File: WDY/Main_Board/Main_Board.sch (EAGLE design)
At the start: 171 parts, among them J1 22-05-7028-02, J10 22-05-7038-03, J11 22-05-7028-02, J12 22-05-7028-02, J13 22-05-7028-02, J14 22-05-7028-02, J15 22-05-7038-03, J2 22-05-7028-02, J3 22-05-7048-04, J4 22-05-7048-04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

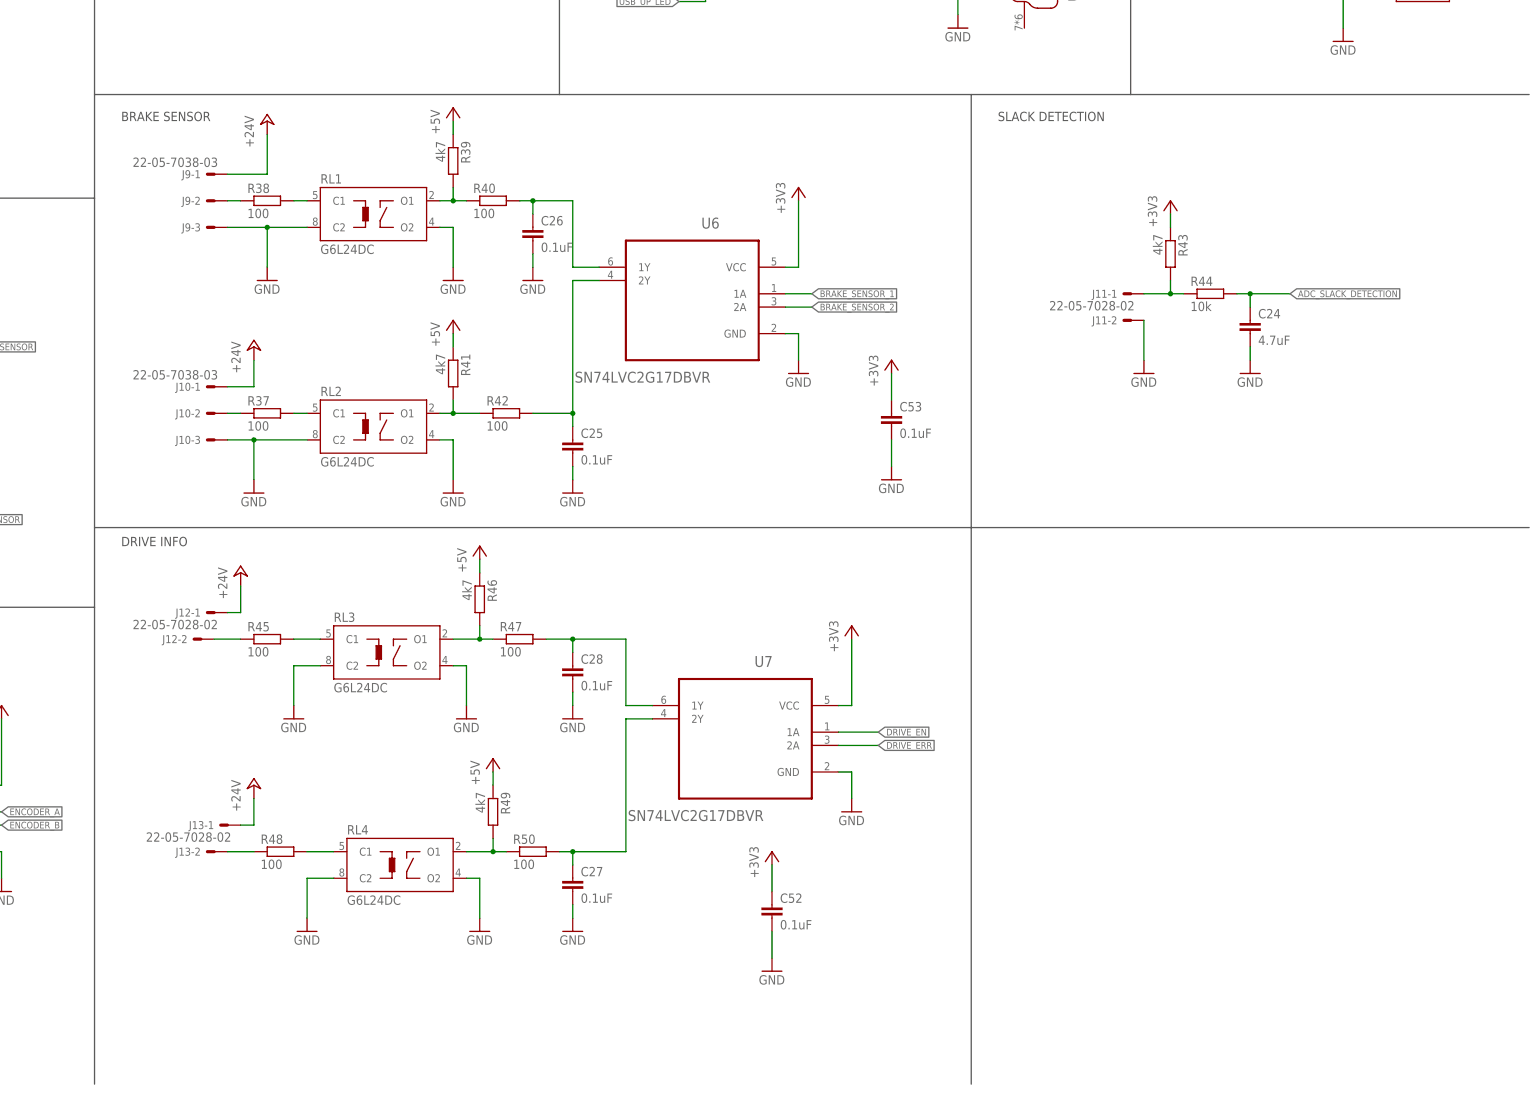
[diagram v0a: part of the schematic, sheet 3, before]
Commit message: Change relay to G6K Place components on the board
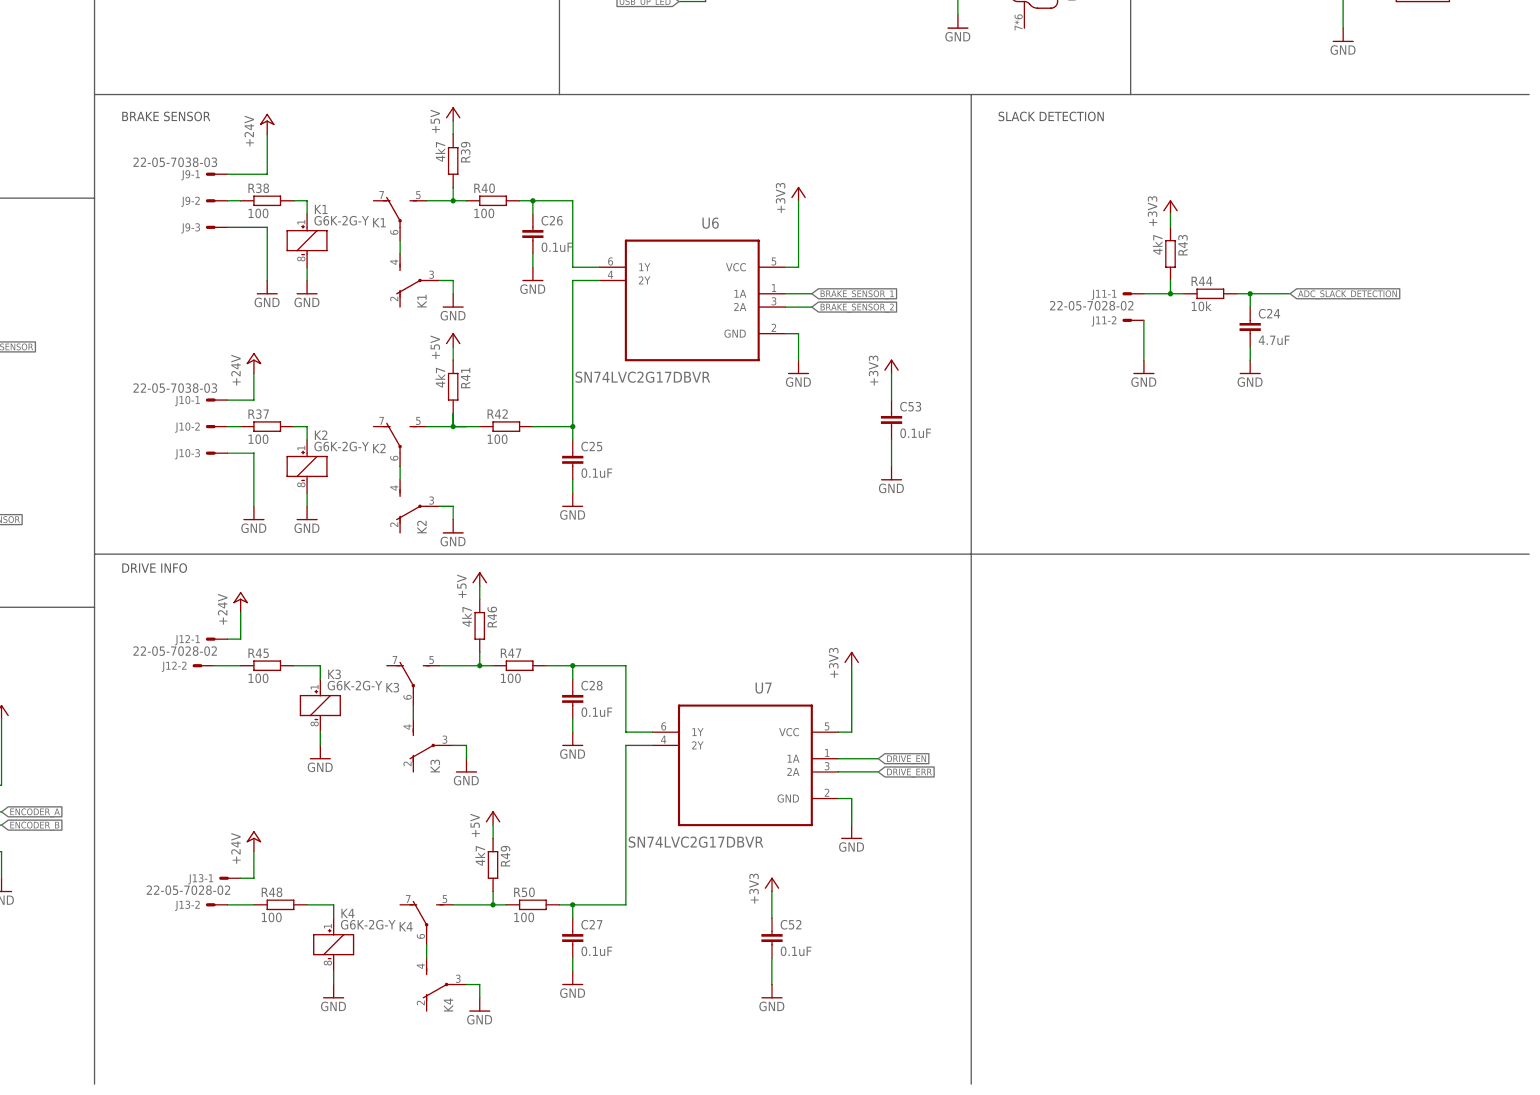
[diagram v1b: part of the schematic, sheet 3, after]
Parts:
- removed RL1, RL2, RL3, RL4: G6L24DC, rel-omron:G6L24DC
- added K1, K2, K3, K4: G6K-2G-Y, relay:G6K-2G-Y
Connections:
- removed net N$35: R48.2, RL4.C1
- new net N$55: K21.+, R37.2
- new net N$57: K22.S, K23.P
- new net N$58: K13.S, R39.2, R40.1
- new net N$59: K42.S, K43.P
- new net N$60: K32.S, K33.P
- net GND: now also K11.-, K12.P, K21.-, K22.P, K31.-, K32.P, K41.-, K42.P; no longer RL1.C2, RL1.O2, RL2.C2, RL2.O2, RL3.C2, RL3.O2, RL4.C2, RL4.O2
- net N$24: now also K11.+; no longer RL1.C1
- net N$28: now also K31.+, R45.2; no longer R37.2, RL2.C1
- net N$29: now also K12.S, K13.P; no longer R39.2, R40.1, RL1.O1
- net N$30: now also K23.S; no longer RL2.O1
- net N$33: now also K41.+, R48.2; no longer R45.2, RL3.C1
- net N$34: now also K33.S; no longer RL3.O1
- net N$36: now also K43.S; no longer RL4.O1
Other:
- moved on the sheet: C25, C27, C28, C52, J10-1, J10-2, J10-3, J12-1, J12-2, J13-1, J13-2, R37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

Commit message: Add Encoder channel Z
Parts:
- removed U10: SN74LVC2G17DBVR, ti:SN74LVC2G17DBVR
- added C54: 0.1uF, rcl:C-EUC0603
- added R60: 100, rcl:R-EU_R0603
- added R61: 4k7, rcl:R-EU_R0603
- added U11: SN74LVC3G17DCTR, ti:SN74LVC3G17DCTR
- J15: value 22-05-7038-03 -> 22-05-7058-05; device con-molex:22-05-7038-03 -> con-molex:22-05-7058-05
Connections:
- net N$40 renamed VIN
- new net ENCODER_Z: U1.P2[8]/TD2/TXD2, U11.3Y
- new net N$35: J15-2.S, R56.2, R57.1
- new net N$40: J15-3.S, R59.1, R61.2
- new net N$62: J15-5.S
- net +3V3: now also U11.VCC; no longer U10.VCC
- net +5V: now also J15-1.S, R61.1
- net ENCODER_A: now also U1.P2[6]/PCAP1[0]/RI1/TRACECLK, U11.1Y; no longer U1.P0[8]/I2STX_WS/MISO1/MAT2[2], U10.1A
- net ENCODER_B: now also U1.P2[7]/RD2/RTS1, U11.2Y; no longer U1.P0[9]/I2STX_SDA/MOSI1/MAT2[3], U10.2A
- net GND: now also C54.2, U11.GND; no longer J15-3.S, U10.GND
- net N$46: now also J15-4.S, R58.2, R60.1; no longer J15-1.S, R56.2, R57.1
- net N$52: now also C54.1, R60.2, U11.3A; no longer J15-2.S, R58.2, R59.1
- net N$53: now also R59.2, U11.2A; no longer R57.2, U10.1Y
- net N$54: now also R57.2, U11.1A; no longer R59.2, U10.2Y
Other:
- moved on the sheet: C24, C25, C26, C27, C28, C46, C47, C51, C52, C53, J10-1, J10-2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
